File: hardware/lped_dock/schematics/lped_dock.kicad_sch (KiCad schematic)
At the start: 1 part

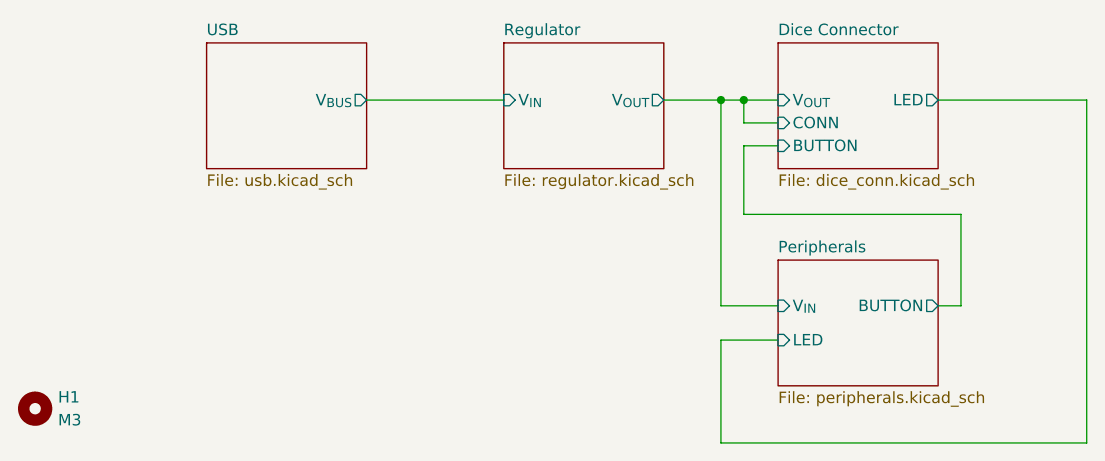
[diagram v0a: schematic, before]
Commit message: feat(hardware): remove unused parts from dock pcb
* Removed LED from dock
* Removed button from dock
* Removed connection pins for LED and button
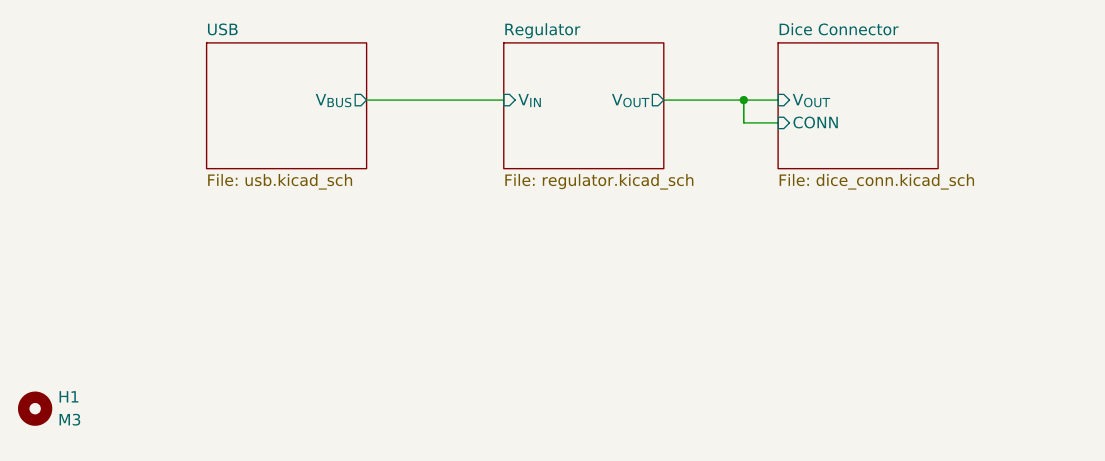
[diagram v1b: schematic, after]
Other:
- removed sheet Peripherals
- sheet Dice Connector ports: added none; removed BUTTON, LED
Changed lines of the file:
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@@
 		(color 0 0 0 0)
 	)
-	(junction
-		(at 149.86 83.82)
-		(diameter 0)
-		(color 0 0 0 0)
-	)
-	(wire
-		(pts
-			(xy 149.86 83.82) (xy 149.86 106.68)
-		)
-		(stroke
-			(width 0)
-			(type default)
-		)
-	)
-	(wire
-		(pts
-			(xy 190.5 83.82) (xy 190.5 121.92)
-		)
-		(stroke
-			(width 0)
-			(type default)
-		)
-	)
-	(wire
-		(pts
-			(xy 149.86 83.82) (xy 152.4 83.82)
-		)
-		(stroke
-			(width 0)
-			(type default)
-		)
-	)
-	(wire
-		(pts
-			(xy 149.86 110.49) (xy 149.86 121.92)
-		)
-		(stroke
-			(width 0)
-			(type default)
-		)
-	)
 	(wire
 		(pts
@@
 	(wire
 		(pts
-			(xy 176.53 106.68) (xy 176.53 96.52)
-		)
-		(stroke
-			(width 0)
-			(type default)
-		)
-	)
-	(wire
-		(pts
 			(xy 152.4 86.36) (xy 156.21 86.36)
 		)
@@
 	(wire
 		(pts
-			(xy 143.51 83.82) (xy 149.86 83.82)
+			(xy 143.51 83.82) (xy 152.4 83.82)
 		)
 		(stroke
@@
 		(pts
 			(xy 110.49 83.82) (xy 125.73 83.82)
-		)
-		(stroke
-			(width 0)
-			(type default)
-		)
-	)
-	(wire
-		(pts
-			(xy 152.4 96.52) (xy 152.4 88.9)
-		)
-		(stroke
-			(width 0)
-			(type default)
-		)
-	)
-	(wire
-		(pts
-			(xy 176.53 96.52) (xy 152.4 96.52)
-		)
-		(stroke
-			(width 0)
-			(type default)
-		)
-	)
-	(wire
-		(pts
-			(xy 149.86 121.92) (xy 190.5 121.92)
-		)
-		(stroke
-			(width 0)
-			(type default)
-		)
-	)
-	(wire
-		(pts
-			(xy 173.99 83.82) (xy 190.5 83.82)
-		)
-		(stroke
-			(width 0)
-			(type default)
-		)
-	)
-	(wire
-		(pts
-			(xy 149.86 106.68) (xy 156.21 106.68)
-		)
-		(stroke
-			(width 0)
-			(type default)
-		)
-	)
-	(wire
-		(pts
-			(xy 173.99 106.68) (xy 176.53 106.68)
-		)
-		(stroke
-			(width 0)
-			(type default)
-		)
-	)
-	(wire
-		(pts
-			(xy 152.4 88.9) (xy 156.21 88.9)
-		)
-		(stroke
-			(width 0)
-			(type default)
-		)
-	)
-	(wire
-		(pts
-			(xy 156.21 110.49) (xy 149.86 110.49)
 		)
 		(stroke
@@
 	)
 	(sheet
-		(at 156.21 101.6)
-		(size 17.78 13.97)
-		(exclude_from_sim no)
-		(in_bom yes)
-		(on_board yes)
-		(dnp no)
-		(fields_autoplaced yes)
-		(stroke
-			(width 0.1524)
-			(type solid)
-		)
-		(fill
-			(color 0 0 0 0.0000)
-		)
-		(property "Sheetname" "Peripherals"
-			(at 156.21 100.8884 0)
-			(effects
-				(font
-					(size 1.27 1.27)
-				)
-				(justify left bottom)
-			)
-		)
-		(property "Sheetfile" "peripherals.kicad_sch"
-			(at 156.21 116.1546 0)
-			(effects
-				(font
-					(size 1.27 1.27)
-				)
-				(justify left top)
-			)
-		)
-		(pin "BUTTON" output
-			(at 173.99 106.68 0)
-			(effects
-				(font
-					(size 1.27 1.27)
-				)
-				(justify right)
-			)
-		)
-		(pin "LED" input
-			(at 156.21 110.49 180)
-			(effects
-				(font
-					(size 1.27 1.27)
-				)
-				(justify left)
-			)
-		)
-		(pin "V_{IN}" input
-			(at 156.21 106.68 180)
-			(effects
-				(font
-					(size 1.27 1.27)
-				)
-				(justify left)
-			)
-		)
-		(instances
-			(project "lped_dock"
-				(path "/5c78e66f-0328-4fd7-bcaa-ded4a2671f1d"
-					(page "5")
-				)
-			)
-		)
-	)
-	(sheet
 		(at 156.21 77.47)
 		(size 17.78 13.97)
@@
 			)
 		)
-		(pin "LED" output
-			(at 173.99 83.82 0)
-			(effects
-				(font
-					(size 1.27 1.27)
-				)
-				(justify right)
-			)
-		)
 		(pin "CONN" input
 			(at 156.21 86.36 180)
 			(effects
 				(font
-					(size 1.27 1.27)
-				)
-				(justify left)
-			)
-		)
-		(pin "BUTTON" input
-			(at 156.21 88.9 180)
-			(effects
-				(font
